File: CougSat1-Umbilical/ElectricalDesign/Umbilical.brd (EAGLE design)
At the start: 49 x 48 mm, 55 parts, among them J1 USB, J2 Umbilical, J3 5V input, Q1 CSD16406Q3, Q2 CSD16406Q3, U1 FT230XQ, U2 BQ24650

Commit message: Added Three M2 Holes
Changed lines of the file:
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@@
 <layer number="43" name="vRestrict" color="2" fill="10" visible="no" active="yes"/>
 <layer number="44" name="Drills" color="7" fill="1" visible="no" active="yes"/>
-<layer number="45" name="Holes" color="7" fill="1" visible="no" active="yes"/>
+<layer number="45" name="Holes" color="7" fill="1" visible="yes" active="yes"/>
 <layer number="46" name="Milling" color="3" fill="1" visible="no" active="yes"/>
 <layer number="47" name="Measures" color="7" fill="1" visible="no" active="yes"/>
@@
 <wire x1="12.7" y1="20.5" x2="13.3" y2="19.9" width="0.1524" layer="21"/>
 <wire x1="12.7" y1="20.5" x2="12.1" y2="19.9" width="0.1524" layer="21"/>
+<hole x="12.5" y="45.5" drill="2"/>
+<hole x="31.9" y="45.5" drill="2"/>
+<hole x="23.8" y="4" drill="2"/>
 </plain>
 <attributes>

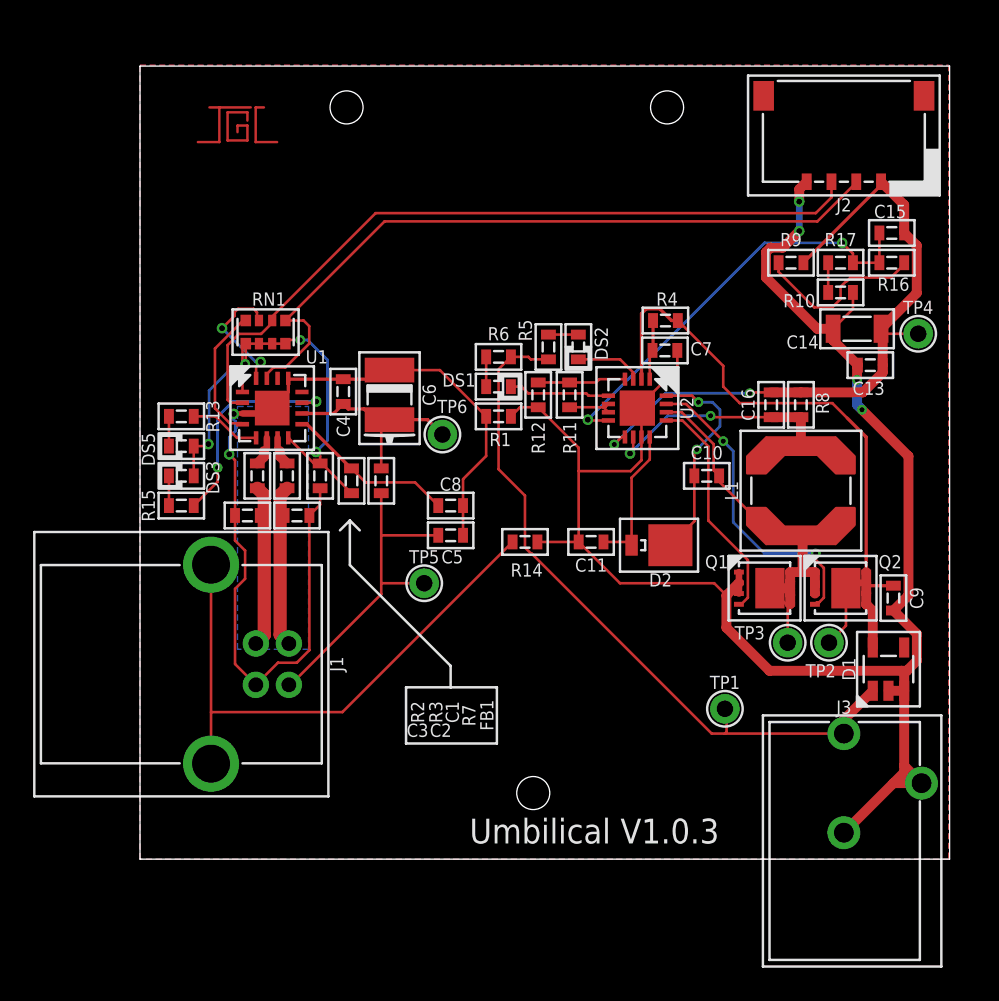
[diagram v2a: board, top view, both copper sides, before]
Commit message: Fixed Mounting Holes And Pico Lock
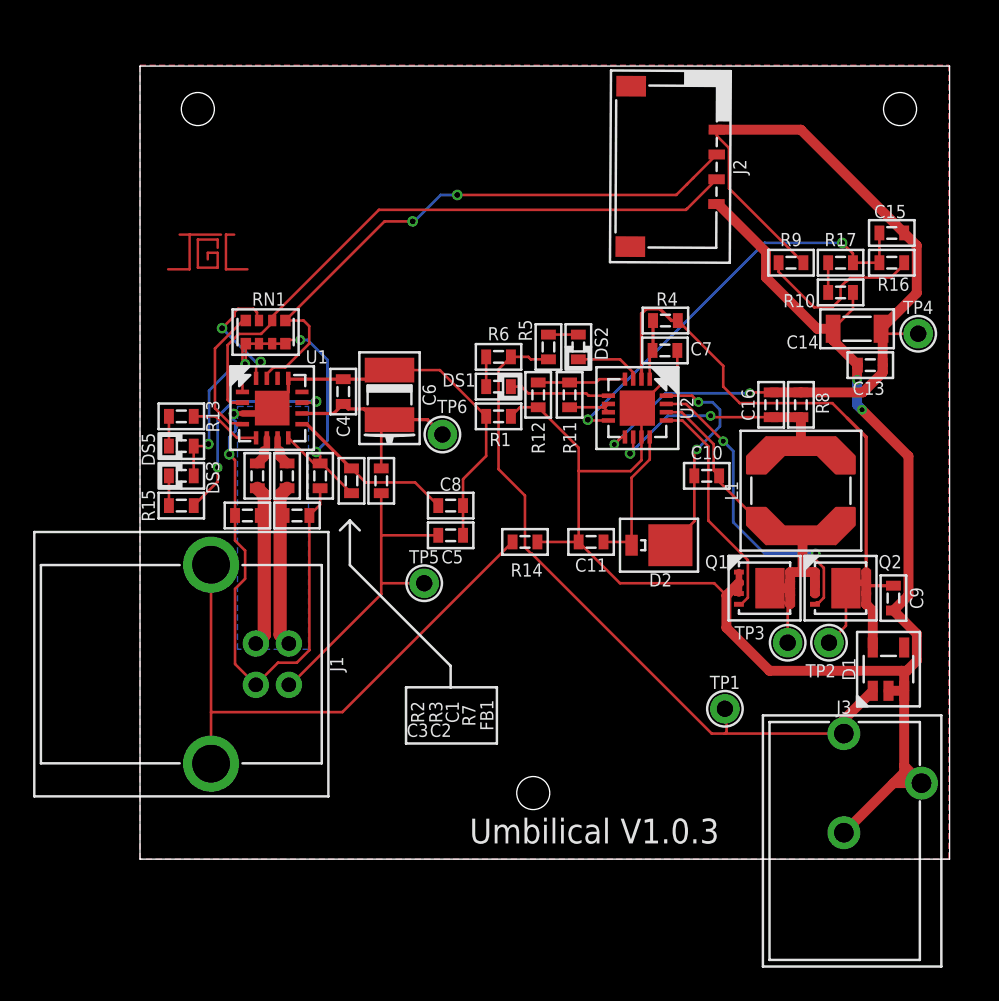
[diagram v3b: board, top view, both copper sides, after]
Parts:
- moved LOGO1 7.91 mm to (4.10, 36.7)
- moved J2 7.75 mm to (34.9, 41.9), turned to 89.7 degrees
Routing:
- net UMB_OUT: track 41.6 -> 55.1 mm
- net UMB_RX: track 44.3 -> 36.5 mm, vias 0 -> 2
- net UMB_TX: track 45.9 -> 38.5 mm
- net PGND: track 106.9 -> 105.4 mm, vias 4 -> 2
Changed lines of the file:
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@@
 <wire x1="12.7" y1="20.5" x2="13.3" y2="19.9" width="0.1524" layer="21"/>
 <wire x1="12.7" y1="20.5" x2="12.1" y2="19.9" width="0.1524" layer="21"/>
-<hole x="12.5" y="45.5" drill="2"/>
-<hole x="31.9" y="45.5" drill="2"/>
+<hole x="3.5" y="45.4" drill="2"/>
+<hole x="46" y="45.4" drill="2"/>
 <hole x="23.8" y="4" drill="2"/>
 </plain>
@@
 <attribute name="SKU" value="05-0004" x="-7.13" y="-9.79" size="1.778" layer="27" rot="R270" display="off"/>
 </element>
-<element name="J2" library="CougsInSpace-Connectors" package="PICOLOCK1.5-04" value="Umbilical" x="42.6" y="41" smashed="yes">
-<attribute name="NAME" x="42.6" y="39.60000625" size="0.8" layer="25" font="vector" ratio="15" align="center"/>
-<attribute name="PACKAGE" value="PicoLock" x="61.649996875" y="18.14000625" size="1.778" layer="27" display="off"/>
-<attribute name="SKU" value="04-0001" x="61.649996875" y="18.14000625" size="1.778" layer="27" display="off"/>
+<element name="J2" library="CougsInSpace-Connectors" package="PICOLOCK1.5-04" value="Umbilical" x="34.9" y="41.9" smashed="yes" rot="R89.7">
+<attribute name="NAME" x="36.299975" y="41.8926625" size="0.8" layer="25" font="vector" ratio="15" rot="R89.7" align="center"/>
+<attribute name="PACKAGE" value="PicoLock" x="57.859425" y="60.8300375" size="1.778" layer="27" rot="R89.7" display="off"/>
+<attribute name="SKU" value="04-0001" x="57.859425" y="60.8300375" size="1.778" layer="27" rot="R89.7" display="off"/>
 </element>
 <element name="J3" library="CougsInSpace-Connectors" package="BARREL-2.1X5.5-R" value="5V input" x="42.6" y="4.6" smashed="yes" rot="R180">
@@
 <attribute name="TEMP" value="70°C Max 2A" x="42.4" y="36.1" size="1.778" layer="27" display="off"/>
 </element>
-<element name="LOGO1" library="CougsInSpace-Aesthetics" package="SIGN-JAYSON" value="SIGNATUREJAYSON" x="5.9" y="44.4" smashed="yes"/>
+<element name="LOGO1" library="CougsInSpace-Aesthetics" package="SIGN-JAYSON" value="SIGNATUREJAYSON" x="4.1" y="36.7" smashed="yes"/>
 </elements>
 <signals>
@@
 <contactref element="R1" pad="2"/>
 <contactref element="R14" pad="2"/>
-<via x="39.9" y="39.8" extent="1-16" drill="0.35"/>
-<via x="39.9" y="38.015" extent="1-16" drill="0.35"/>
-<wire x1="39.9" y1="39.8" x2="39.9" y2="38.015" width="0.4" layer="16"/>
 <wire x1="36.25" y1="17.375" x2="36.25" y2="16.725" width="0.4" layer="1"/>
 <wire x1="36.25" y1="16.725" x2="36.25" y2="16.075" width="0.4" layer="1"/>
@@
 <wire x1="43.45" y1="29.9" x2="41.95" y2="31.4" width="0.6" layer="1"/>
 <wire x1="41.95" y1="31.4" x2="41.95" y2="32.1" width="0.6" layer="1"/>
-<wire x1="37.89" y1="36.7405375" x2="38.1594625" y2="37.01" width="0.6" layer="1"/>
-<wire x1="38.1594625" y1="37.01" x2="38.895" y2="37.01" width="0.6" layer="1"/>
-<wire x1="38.895" y1="37.01" x2="39.9" y2="38.015" width="0.6" layer="1"/>
 <wire x1="37.89" y1="36.7405375" x2="37.89" y2="35.1998375" width="0.6" layer="1"/>
 <wire x1="40.9898375" y1="32.1" x2="41.95" y2="32.1" width="0.6" layer="1"/>
@@
 <wire x1="30.35" y1="25.55" x2="30.35" y2="27.05" width="0.16" layer="1"/>
 <wire x1="30.35" y1="27.05" x2="30.1" y2="27.3" width="0.16" layer="1"/>
-<wire x1="39.9" y1="39.8" x2="39.9" y2="40.55" width="0.6" layer="1"/>
-<wire x1="39.9" y1="40.55" x2="40.35" y2="41" width="0.6" layer="1"/>
 <wire x1="24.1" y1="27.35" x2="23" y2="27.35" width="0.16" layer="1"/>
 <wire x1="23" y1="27.35" x2="22.45" y2="26.8" width="0.16" layer="1"/>
@@
 <wire x1="43.15" y1="34.3" x2="43.15" y2="33.3" width="0.16" layer="1"/>
 <wire x1="43.15" y1="33.3" x2="41.95" y2="32.1" width="0.16" layer="1"/>
+<wire x1="34.88821875" y1="39.650028125" x2="34.980509375" y2="39.650028125" width="0.6" layer="1"/>
+<wire x1="34.980509375" y1="39.650028125" x2="37.89" y2="36.7405375" width="0.6" layer="1"/>
 </signal>
 <signal name="DIODE_OUT">
@@
 <contactref element="R8" pad="2"/>
 <contactref element="TP4" pad="1"/>
-<wire x1="44.85" y1="41" x2="44.925" y2="40.925" width="0.2" layer="1"/>
-<wire x1="40.15" y1="36.1" x2="44.925" y2="40.875" width="0.2" layer="1"/>
-<wire x1="44.925" y1="40.875" x2="44.925" y2="40.925" width="0.2" layer="1"/>
 <via x="36.9" y="28.2" extent="1-16" drill="0.3"/>
 <wire x1="36.9" y1="28.2" x2="31.8" y2="28.2" width="0.16" layer="16"/>
@@
 <wire x1="47.01" y1="37.14" x2="46.25" y2="37.9" width="0.6" layer="1"/>
 <wire x1="47.01" y1="34.26" x2="47.01" y2="37.14" width="0.6" layer="1"/>
-<wire x1="46.25" y1="37.9" x2="46.25" y2="39.6" width="0.6" layer="1"/>
-<wire x1="46.25" y1="39.6" x2="44.85" y2="41" width="0.6" layer="1"/>
 <wire x1="36.9" y1="28.2" x2="36.95" y2="28.25" width="0.16" layer="1"/>
 <wire x1="36.95" y1="28.25" x2="38.2" y2="28.25" width="0.16" layer="1"/>
@@
 <wire x1="45.2" y1="31.8" x2="47.1" y2="31.8" width="0.16" layer="1"/>
 <wire x1="45.2" y1="31.8" x2="44.9" y2="32.1" width="0.16" layer="1"/>
+<wire x1="34.911778125" y1="43.78121875" x2="34.911778125" y2="44.14996875" width="0.16" layer="1"/>
+<wire x1="35.64600625" y1="43.046990625" x2="34.911778125" y2="43.78121875" width="0.16" layer="1"/>
+<wire x1="40.15" y1="36.1" x2="35.64600625" y2="40.60399375" width="0.16" layer="1"/>
+<wire x1="35.64600625" y1="40.60399375" x2="35.64600625" y2="43.046990625" width="0.16" layer="1"/>
+<wire x1="34.911778125" y1="44.14996875" x2="40.00003125" y2="44.14996875" width="0.6" layer="1"/>
+<wire x1="40.00003125" y1="44.14996875" x2="46.25" y2="37.9" width="0.6" layer="1"/>
 </signal>
 <signal name="UMB_RX">
@@
 <contactref element="U1" pad="15"/>
 <contactref element="RN1" pad="1"/>
-<wire x1="8.8" y1="32.6" x2="14.8" y2="38.6" width="0.16" layer="1"/>
-<wire x1="14.8" y1="38.6" x2="41" y2="38.6" width="0.16" layer="1"/>
-<wire x1="41" y1="38.6" x2="43.35" y2="40.95" width="0.16" layer="1"/>
-<wire x1="43.35" y1="40.95" x2="43.35" y2="41" width="0.2" layer="1"/>
+<wire x1="14.8" y1="38.6" x2="8.8" y2="32.6" width="0.16" layer="1"/>
 <wire x1="8.8" y1="32.6" x2="9.9" y2="32.6" width="0.16" layer="1"/>
 <wire x1="9.9" y1="32.6" x2="10.24" y2="32.26" width="0.16" layer="1"/>
@@
 <wire x1="8.07730625" y1="29.76" x2="8.79868125" y2="29.76" width="0.16" layer="1"/>
 <wire x1="8.79868125" y1="29.76" x2="10.24" y2="31.20131875" width="0.16" layer="1"/>
+<wire x1="34.903925" y1="42.6499875" x2="33.47696875" y2="41.22303125" width="0.16" layer="1"/>
+<wire x1="33.47696875" y1="41.22303125" x2="33.103925" y2="40.8499875" width="0.16" layer="1"/>
+<wire x1="16.5" y1="38.6" x2="16.6" y2="38.6" width="0.16" layer="16"/>
+<via x="16.5" y="38.6" extent="1-16" drill="0.35"/>
+<wire x1="16.5" y1="38.6" x2="14.8" y2="38.6" width="0.16" layer="1"/>
+<wire x1="18.2" y1="40.2" x2="19.2" y2="40.2" width="0.16" layer="16"/>
+<via x="19.2" y="40.2" extent="1-16" drill="0.35"/>
+<wire x1="19.2" y1="40.2" x2="32.4539375" y2="40.2" width="0.16" layer="1"/>
+<wire x1="32.4539375" y1="40.2" x2="33.103925" y2="40.8499875" width="0.16" layer="1"/>
+<wire x1="16.6" y1="38.6" x2="18.2" y2="40.2" width="0.16" layer="16"/>
 </signal>
 <signal name="UMB_TX">
@@
 <contactref element="J2" pad="3"/>
 <contactref element="RN1" pad="2"/>
-<wire x1="41.85" y1="41" x2="41.85" y2="40.05" width="0.16" layer="1"/>
-<wire x1="41.85" y1="40.05" x2="40.9" y2="39.1" width="0.16" layer="1"/>
 <wire x1="8" y1="32.83769375" x2="8" y2="32.6" width="0.16" layer="1"/>
-<wire x1="40.9" y1="39.1" x2="14.26230625" y2="39.1" width="0.16" layer="1"/>
-<wire x1="14.26230625" y1="39.1" x2="8" y2="32.83769375" width="0.16" layer="1"/>
+<wire x1="14.46230625" y1="39.3" x2="8" y2="32.83769375" width="0.16" layer="1"/>
 <wire x1="7.3294125" y1="31.79" x2="8" y2="32.4605875" width="0.16" layer="1"/>
 <wire x1="5.9805875" y1="31.79" x2="7.3294125" y2="31.79" width="0.16" layer="1"/>
@@
 <wire x1="5.3" y1="27.8" x2="5.3" y2="31.1094125" width="0.16" layer="1"/>
 <wire x1="5.3" y1="31.1094125" x2="5.9805875" y2="31.79" width="0.16" layer="1"/>
+<wire x1="34.896071875" y1="41.150009375" x2="33.12303125" y2="39.37696875" width="0.16" layer="1"/>
+<wire x1="33.12303125" y1="39.37696875" x2="33.0460625" y2="39.3" width="0.16" layer="1"/>
+<wire x1="33.0460625" y1="39.3" x2="14.46230625" y2="39.3" width="0.16" layer="1"/>
 </signal>
 <signal name="3.3V">
@@
 <contactref element="C6" pad="A"/>
 <contactref element="TP6" pad="1"/>
-<wire x1="14.6" y1="23.65" x2="14.6" y2="26.1" width="0.16" layer="1"/>
 <wire x1="14.6" y1="26.1" x2="14.65" y2="26.15" width="0.2" layer="1"/>
-<wire x1="15" y1="26.5" x2="15.1" y2="26.6" width="0.2" layer="1"/>
 <wire x1="12.3" y1="27.55" x2="11.725" y2="26.975" width="0.2" layer="1"/>
 <wire x1="11.725" y1="26.975" x2="9.8" y2="26.975" width="0.2" layer="1"/>
@@
 <wire x1="15.1" y1="26.6" x2="17.4" y2="26.6" width="0.2" layer="1"/>
 <wire x1="17.4" y1="26.6" x2="18.3" y2="25.7" width="0.2" layer="1"/>
-<wire x1="14.6" y1="23.65" x2="15" y2="26.5" width="0" layer="19" extent="1-1"/>
+<wire x1="15" y1="26.5" x2="14.65" y2="26.15" width="0.16" layer="1"/>
+<wire x1="14.6" y1="23.65" x2="14.6" y2="26.1" width="0.16" layer="1"/>
+<wire x1="15.1" y1="26.6" x2="15" y2="26.5" width="0.16" layer="1"/>
 </signal>
 <signal name="USB5V">

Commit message: Changed Board Size
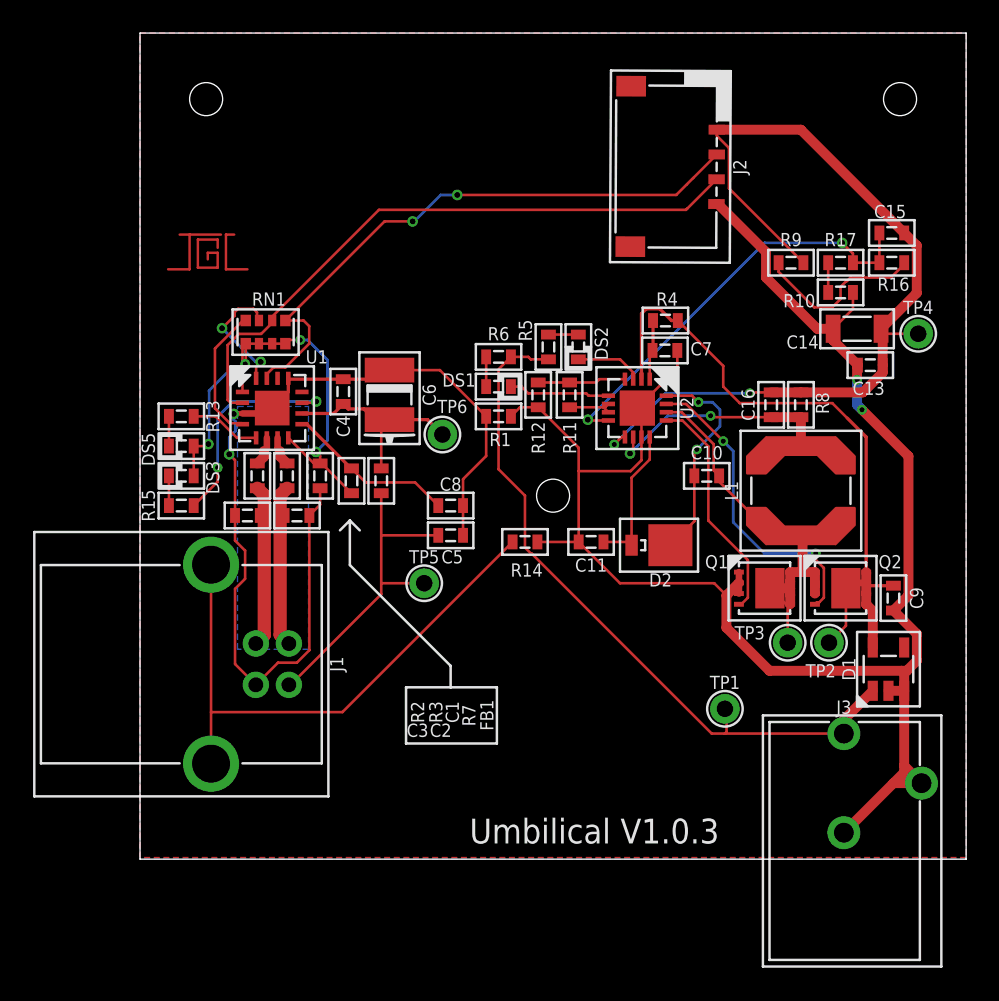
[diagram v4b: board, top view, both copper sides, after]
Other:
- board size 49 x 48 mm -> 50 x 50 mm
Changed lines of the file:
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@@
 <board>
 <plain>
-<wire x1="0" y1="0" x2="49" y2="0" width="0" layer="20"/>
-<wire x1="49" y1="0" x2="49" y2="48" width="0" layer="20"/>
-<wire x1="49" y1="48" x2="0" y2="48" width="0" layer="20"/>
-<wire x1="0" y1="48" x2="0" y2="0" width="0" layer="20"/>
+<wire x1="0" y1="0" x2="50" y2="0" width="0" layer="20"/>
+<wire x1="50" y1="0" x2="50" y2="50" width="0" layer="20"/>
+<wire x1="50" y1="50" x2="0" y2="50" width="0" layer="20"/>
+<wire x1="0" y1="50" x2="0" y2="0" width="0" layer="20"/>
 <text x="27.5" y="1.7" size="1.5" layer="21" font="vector" ratio="15" rot="R180" align="center">Umbilical V1.0.3</text>
 <wire x1="16.1" y1="10.4" x2="16.1" y2="7" width="0.1524" layer="21"/>
@@
 <wire x1="12.7" y1="20.5" x2="13.3" y2="19.9" width="0.1524" layer="21"/>
 <wire x1="12.7" y1="20.5" x2="12.1" y2="19.9" width="0.1524" layer="21"/>
-<hole x="3.5" y="45.4" drill="2"/>
-<hole x="46" y="45.4" drill="2"/>
-<hole x="23.8" y="4" drill="2"/>
+<hole x="4" y="46" drill="2"/>
+<hole x="46" y="46" drill="2"/>
+<hole x="25" y="22" drill="2"/>
 </plain>
 <attributes>
@@
 <polygon width="0.16" layer="16" spacing="0.5" pour="hatch" rank="6">
 <vertex x="0" y="0"/>
-<vertex x="0" y="48.05"/>
-<vertex x="48.95" y="48.05"/>
-<vertex x="48.95" y="0"/>
+<vertex x="0" y="50"/>
+<vertex x="50" y="50"/>
+<vertex x="50" y="0"/>
 </polygon>
 </signal>
 <signal name="BALANCING-TOP">
 <polygon width="0.16" layer="1" spacing="0.5" pour="hatch" rank="6">
-<vertex x="0" y="0"/>
-<vertex x="0" y="48.05"/>
-<vertex x="48.95" y="48.05"/>
-<vertex x="48.95" y="0"/>
+<vertex x="0" y="0.1"/>
+<vertex x="0" y="50"/>
+<vertex x="50" y="50"/>
+<vertex x="50" y="0.1"/>
 </polygon>
 </signal>
